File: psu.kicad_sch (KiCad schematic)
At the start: 0 parts

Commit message: Add files via upload
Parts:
- added C42: 100u/50V, Capacitor_SMD:CP_Elec_8x10.5, symbol Device:C_Polarized_Small
- added C5 (x2): 22u/6.3V, Capacitor_SMD:C_0603_1608Metric, symbol Device:C_Small
- added C5 (x2): 100n, Capacitor_SMD:C_0603_1608Metric, symbol Device:C_Small
- added J1: Conn_01x01_Pin, TestPoint:TestPoint_Pad_D3.0mm, symbol Connector:Conn_01x01_Pin
- added L1: 10u, Inductor_SMD:L_Vishay_IHLP-2525, symbol Device:L_Small
- added R2: 100k, Resistor_SMD:R_0603_1608Metric, symbol Device:R_Small
- added R2: 75k, Resistor_SMD:R_0603_1608Metric, symbol Device:R_Small
- added R2: 24k, Resistor_SMD:R_0603_1608Metric, symbol Device:R_Small
- added TP2 (x2): ~, TestPoint:TestPoint_Pad_D1.5mm, symbol Connector:TestPoint_Probe
- added U5: ~, Package_TO_SOT_SMD:SOT-23-6, symbol Parts:TP6841S6-A
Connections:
- net 13.8V_OUT: now also C42.1, C5.1, C5.2, J1.1 (Pin_1), R2.1, TP2.1, U5.5 (VIN)
- net 3.3V_OUT: now also C5.2, L1.2, R2.2, TP2.1
- new net: R2.2, U5.4 (EN)
- new net: R2.1, R2.1, U5.3 (FB)
- new net: C5.2, L1.1, U5.6 (SW)
- new net: C5.1, U5.1 (BST)
- new net GND: C42.2, C5.1, C5.1, C5.2, R2.2, U5.2 (GND)
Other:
- note added: "Voltage reg."

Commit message: partial PN update
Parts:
- C5: PN (none) -> C0603C104M5RAC7411
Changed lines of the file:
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@@
         )
         (path "/4c42207c-9e6b-42da-ad38-da126b892014/76d2ec5b-2ec2-4780-ac71-2509ae9f2d67"
-          (reference "TP8") (unit 1)
+          (reference "TP10") (unit 1)
         )
       )
@@
         )
         (path "/4c42207c-9e6b-42da-ad38-da126b892014/76d2ec5b-2ec2-4780-ac71-2509ae9f2d67"
-          (reference "C10") (unit 1)
+          (reference "C11") (unit 1)
         )
       )
@@
       (effects (font (size 1.27 1.27)) hide)
     )
+    (property "PN" "C0603C104M5RAC7411" (at 173.99 152.4 0)
+      (effects (font (size 1.27 1.27)) hide)
+    )
     (pin "1")
     (pin "2")
@@
         )
         (path "/4c42207c-9e6b-42da-ad38-da126b892014/76d2ec5b-2ec2-4780-ac71-2509ae9f2d67"
-          (reference "C11") (unit 1)
+          (reference "C12") (unit 1)
         )
       )
@@
         )
         (path "/4c42207c-9e6b-42da-ad38-da126b892014/76d2ec5b-2ec2-4780-ac71-2509ae9f2d67"
-          (reference "TP9") (unit 1)
+          (reference "TP11") (unit 1)
         )
       )
@@
         )
         (path "/4c42207c-9e6b-42da-ad38-da126b892014/76d2ec5b-2ec2-4780-ac71-2509ae9f2d67"
-          (reference "C14") (unit 1)
+          (reference "C15") (unit 1)
         )
       )
@@
         )
         (path "/4c42207c-9e6b-42da-ad38-da126b892014/76d2ec5b-2ec2-4780-ac71-2509ae9f2d67"
+          (reference "C14") (unit 1)
+        )
+      )
+    )
+  )
+  (symbol (lib_id "Connector:Conn_01x01_Pin") (at 156.21 123.19 0) (unit 1)
+    (in_bom yes) (on_board yes) (dnp no) (fields_autoplaced)
+    (property "Reference" "J1" (at 156.845 118.9695 0)
+      (effects (font (size 1.27 1.27)))
+    )
+    (property "Value" "Conn_01x01_Pin" (at 156.845 121.3937 0)
+      (effects (font (size 1.27 1.27)))
+    )
+    (property "Footprint" "TestPoint:TestPoint_Pad_D3.0mm" (at 156.21 123.19 0)
+      (effects (font (size 1.27 1.27)) hide)
+    )
+    (property "Datasheet" "~" (at 156.21 123.19 0)
+      (effects (font (size 1.27 1.27)) hide)
+    )
+    (pin "1")
+    (instances
+      (project "m17-rru-rf"
+        (path "/4c42207c-9e6b-42da-ad38-da126b892014/76d2ec5b-2ec2-4780-ac71-2509ae9f2d67"
+          (reference "J1") (unit 1)
+        )
+      )
+    )
+  )
+  (symbol (lib_id "Device:C_Small") (at 207.01 134.62 90) (unit 1)
+    (in_bom yes) (on_board yes) (dnp no) (fields_autoplaced)
+    (property "Reference" "C5" (at 207.0163 128.9136 90)
+      (effects (font (size 1.27 1.27)))
+    )
+    (property "Value" "100n" (at 207.0163 131.3378 90)
+      (effects (font (size 1.27 1.27)))
+    )
+    (property "Footprint" "Capacitor_SMD:C_0603_1608Metric" (at 207.01 134.62 0)
+      (effects (font (size 1.27 1.27)) hide)
+    )
+    (property "Datasheet" "~" (at 207.01 134.62 0)
+      (effects (font (size 1.27 1.27)) hide)
+    )
+    (property "PN" "C0603C104M5RAC7411" (at 207.01 134.62 0)
+      (effects (font (size 1.27 1.27)) hide)
+    )
+    (pin "1")
+    (pin "2")
+    (instances
+      (project "m17-rru-rf"
+        (path "/4c42207c-9e6b-42da-ad38-da126b892014/ccc39fee-262d-4ac9-a9a6-59e024db6eed"
+          (reference "C5") (unit 1)
+        )
+        (path "/4c42207c-9e6b-42da-ad38-da126b892014/7ebe248e-d508-4395-8ad3-4ea02a49e591"
+          (reference "C4") (unit 1)
+        )
+        (path "/4c42207c-9e6b-42da-ad38-da126b892014/8d8271f4-10c0-40f4-bdf8-e0e4dac71cc9"
+          (reference "C28") (unit 1)
+        )
+        (path "/4c42207c-9e6b-42da-ad38-da126b892014/76d2ec5b-2ec2-4780-ac71-2509ae9f2d67"
           (reference "C13") (unit 1)
         )
       )
-    )
-  )
-  (symbol (lib_id "Connector:Conn_01x01_Pin") (at 156.21 123.19 0) (unit 1)
-    (in_bom yes) (on_board yes) (dnp no) (fields_autoplaced)
-    (property "Reference" "J1" (at 156.845 118.9695 0)
-      (effects (font (size 1.27 1.27)))
-    )
-    (property "Value" "Conn_01x01_Pin" (at 156.845 121.3937 0)
-      (effects (font (size 1.27 1.27)))
-    )
-    (property "Footprint" "TestPoint:TestPoint_Pad_D3.0mm" (at 156.21 123.19 0)
-      (effects (font (size 1.27 1.27)) hide)
-    )
-    (property "Datasheet" "~" (at 156.21 123.19 0)
-      (effects (font (size 1.27 1.27)) hide)
-    )
-    (pin "1")
-    (instances
-      (project "m17-rru-rf"
-        (path "/4c42207c-9e6b-42da-ad38-da126b892014/76d2ec5b-2ec2-4780-ac71-2509ae9f2d67"
-          (reference "J1") (unit 1)
-        )
-      )
-    )
-  )
-  (symbol (lib_id "Device:C_Small") (at 207.01 134.62 90) (unit 1)
-    (in_bom yes) (on_board yes) (dnp no) (fields_autoplaced)
-    (property "Reference" "C5" (at 207.0163 128.9136 90)
-      (effects (font (size 1.27 1.27)))
-    )
-    (property "Value" "100n" (at 207.0163 131.3378 90)
-      (effects (font (size 1.27 1.27)))
-    )
-    (property "Footprint" "Capacitor_SMD:C_0603_1608Metric" (at 207.01 134.62 0)
-      (effects (font (size 1.27 1.27)) hide)
-    )
-    (property "Datasheet" "~" (at 207.01 134.62 0)
-      (effects (font (size 1.27 1.27)) hide)
-    )
-    (pin "1")
-    (pin "2")
-    (instances
-      (project "m17-rru-rf"
-        (path "/4c42207c-9e6b-42da-ad38-da126b892014/ccc39fee-262d-4ac9-a9a6-59e024db6eed"
-          (reference "C5") (unit 1)
-        )
-        (path "/4c42207c-9e6b-42da-ad38-da126b892014/7ebe248e-d508-4395-8ad3-4ea02a49e591"
-          (reference "C4") (unit 1)
-        )
-        (path "/4c42207c-9e6b-42da-ad38-da126b892014/8d8271f4-10c0-40f4-bdf8-e0e4dac71cc9"
-          (reference "C28") (unit 1)
-        )
-        (path "/4c42207c-9e6b-42da-ad38-da126b892014/76d2ec5b-2ec2-4780-ac71-2509ae9f2d67"
-          (reference "C12") (unit 1)
-        )
-      )

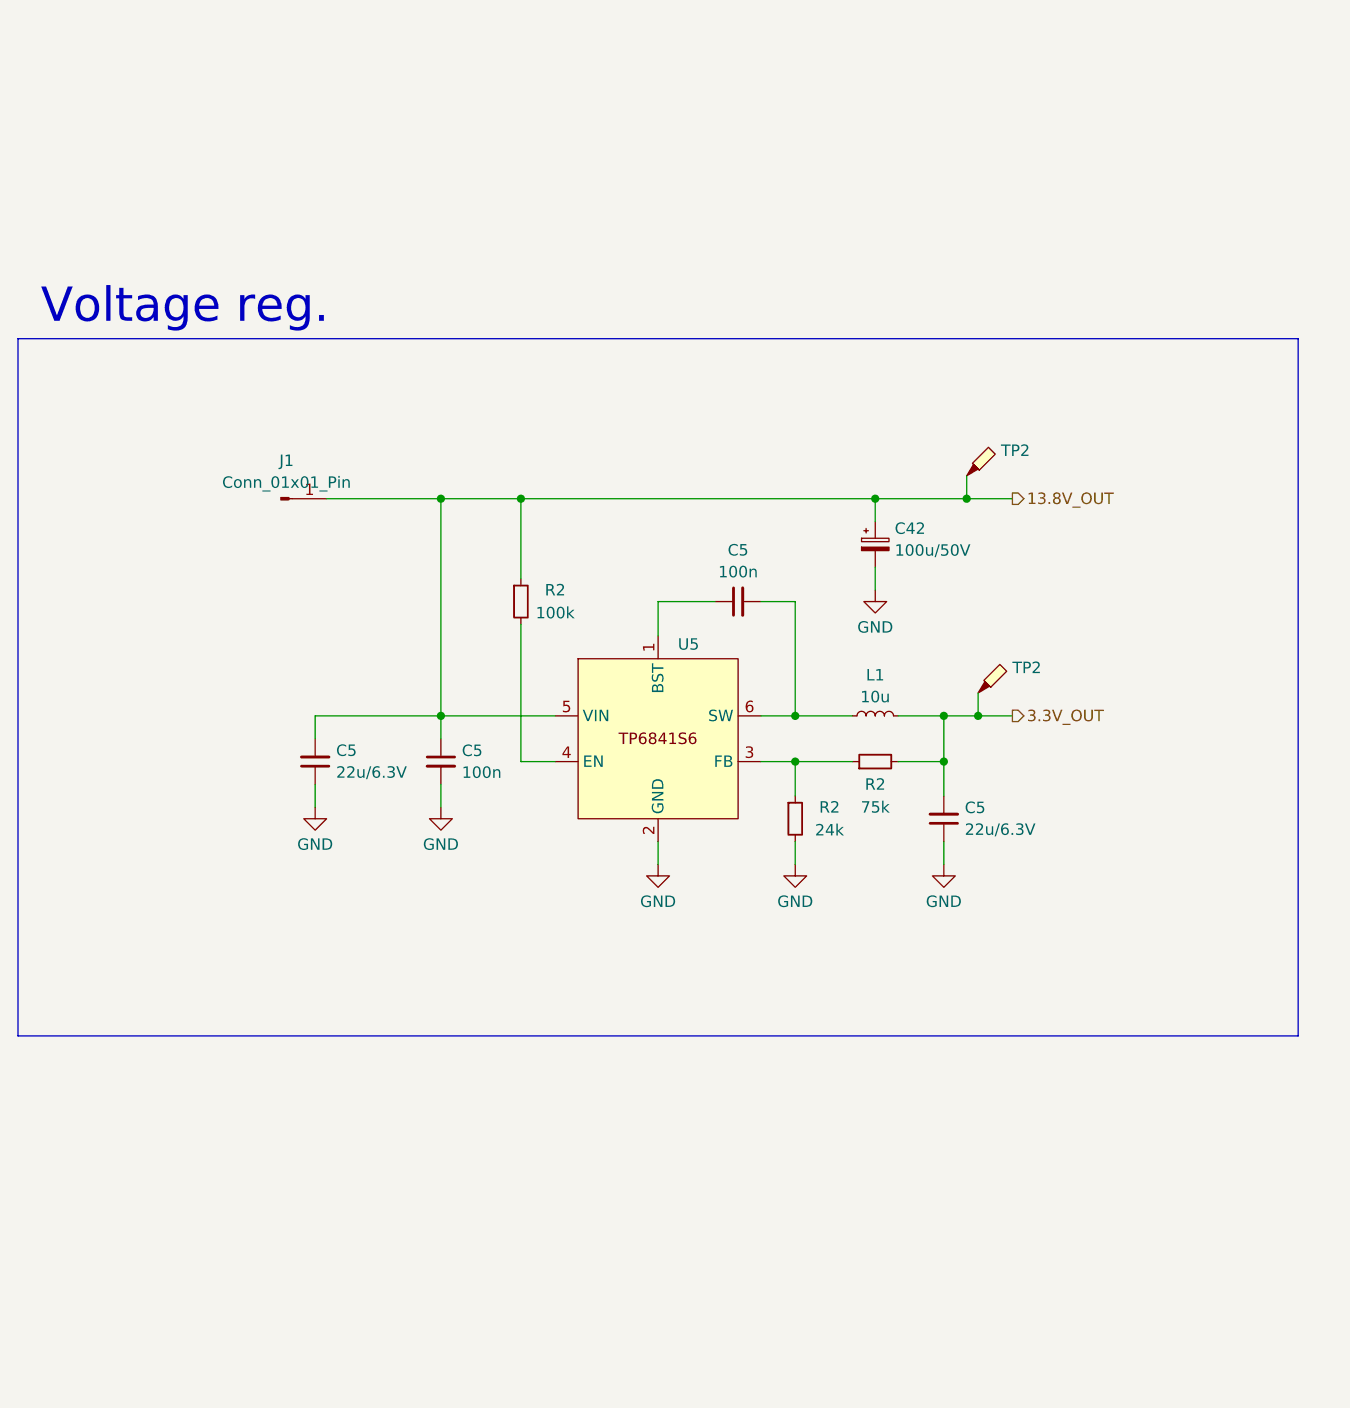
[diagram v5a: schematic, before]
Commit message: significant updates
- supply for the detector block changed from 3.3V to 5V
- minor bugfixes
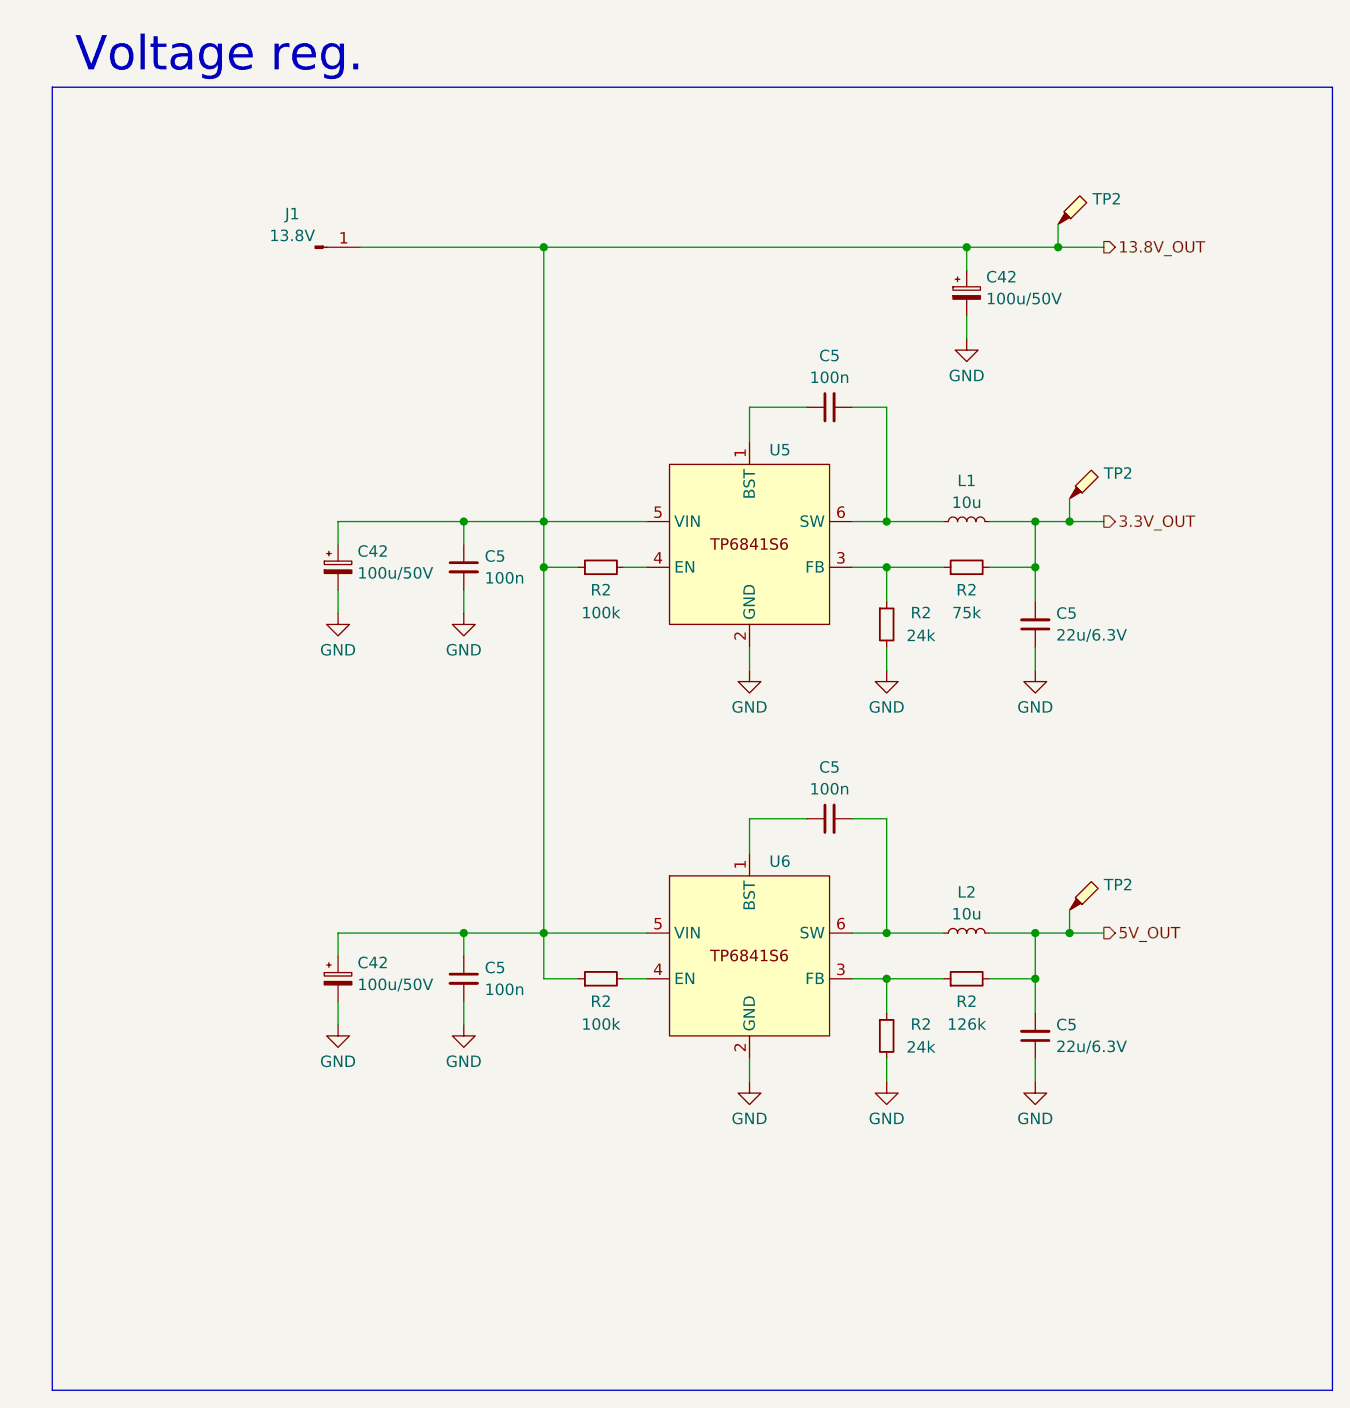
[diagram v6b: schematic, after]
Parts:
- removed C5: 22u/6.3V, Capacitor_SMD:C_0603_1608Metric, symbol Device:C_Small
- added C42 (x2): 100u/50V, Capacitor_SMD:CP_Elec_8x10.5, symbol Device:C_Polarized_Small
- added C5 (x2): 100n, Capacitor_SMD:C_0603_1608Metric, symbol Device:C_Small
- added C5: 22u/6.3V, Capacitor_SMD:C_0603_1608Metric, symbol Device:C_Small
- added L2: 10u, Inductor_SMD:L_Vishay_IHLP-2525, symbol Device:L_Small
- added R2: 126k, Resistor_SMD:R_0603_1608Metric, symbol Device:R_Small
- added R2: 24k, Resistor_SMD:R_0603_1608Metric, symbol Device:R_Small
- added R2: 100k, Resistor_SMD:R_0603_1608Metric, symbol Device:R_Small
- added TP2: ~, TestPoint:TestPoint_Pad_D1.5mm, symbol Connector:TestPoint_Probe
- added U6: ~, Package_TO_SOT_SMD:SOT-23-6, symbol Parts:TP6841S6-A
- J1: value Conn_01x01_Pin -> 13.8V
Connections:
- net 13.8V_OUT: now also C42.1, C42.1, C5.1, R2.1, U6.5 (VIN)
- net GND: now also C42.2, C42.2, C5.1, C5.2, R2.2, U6.2 (GND)
- new net: R2.1, R2.1, U6.3 (FB)
- new net: C5.1, U6.1 (BST)
- new net: C5.2, L2.1, U6.6 (SW)
- new net: R2.2, U6.4 (EN)
- new net 5V_OUT: C5.2, L2.2, R2.2, TP2.1
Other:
- moved on the sheet: C42, C5, J1, L1, R2, TP2, U5

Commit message: PN update
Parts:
- J1: PN (none) -> -
- TP2: value ~ -> TP; PN (none) -> -
- U5, U6: value ~ -> TP6841
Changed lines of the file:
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@@
       (effects (font (size 1.27 1.27)) (justify left))
     )
-    (property "Value" "~" (at 246.38 92.3346 0)
+    (property "Value" "TP" (at 246.38 92.3346 0)
       (effects (font (size 1.27 1.27)) (justify left))
     )
@@
     )
     (property "Datasheet" "~" (at 247.65 92.71 0)
+      (effects (font (size 1.27 1.27)) hide)
+    )
+    (property "PN" "-" (at 242.57 92.71 0)
       (effects (font (size 1.27 1.27)) hide)
     )
@@
       (effects (font (size 1.27 1.27)) (justify left))
     )
-    (property "Value" "~" (at 208.28 173.99 0)
+    (property "Value" "TP6841" (at 208.28 173.99 0)
       (effects (font (size 1.27 1.27)))
     )
@@
       (effects (font (size 1.27 1.27)) (justify left))
     )
-    (property "Value" "~" (at 247.65 122.8146 0)
+    (property "Value" "TP" (at 247.65 122.8146 0)
       (effects (font (size 1.27 1.27)) (justify left))
     )
@@
     )
     (property "Datasheet" "~" (at 248.92 123.19 0)
+      (effects (font (size 1.27 1.27)) hide)
+    )
+    (property "PN" "-" (at 243.84 123.19 0)
       (effects (font (size 1.27 1.27)) hide)
     )
@@
       (effects (font (size 1.27 1.27)) (justify left))
     )
-    (property "Value" "~" (at 247.65 168.5346 0)
+    (property "Value" "TP" (at 247.65 168.5346 0)
       (effects (font (size 1.27 1.27)) (justify left))
     )
@@
     )
     (property "Datasheet" "~" (at 248.92 168.91 0)
+      (effects (font (size 1.27 1.27)) hide)
+    )
+    (property "PN" "-" (at 243.84 168.91 0)
       (effects (font (size 1.27 1.27)) hide)
     )
@@
       (effects (font (size 1.27 1.27)) (justify left))
     )
-    (property "Value" "~" (at 208.28 128.27 0)
+    (property "Value" "TP6841" (at 208.28 128.27 0)
       (effects (font (size 1.27 1.27)))
     )
@@
       (effects (font (size 1.27 1.27)) hide)
     )
+    (property "PN" "-" (at 160.02 95.25 0)
+      (effects (font (size 1.27 1.27)) hide)
+    )
